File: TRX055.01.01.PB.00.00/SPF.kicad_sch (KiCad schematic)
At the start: 1 part, among them J5 SFP

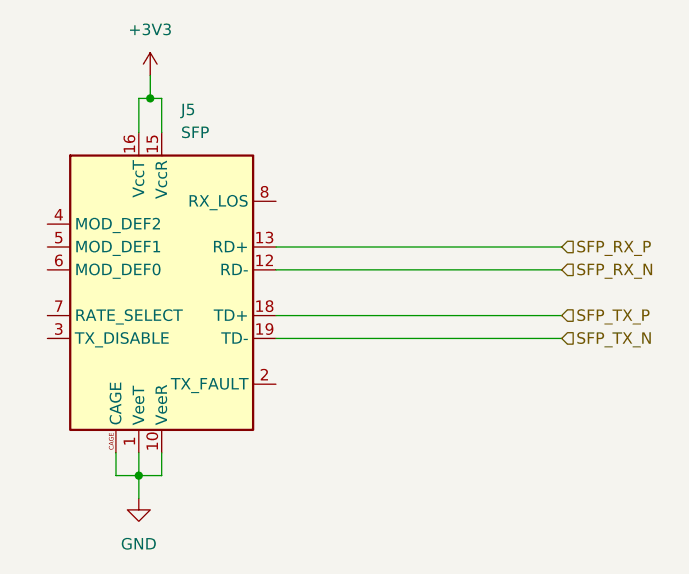
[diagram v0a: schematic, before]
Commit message: +ETH +USB +Connectors
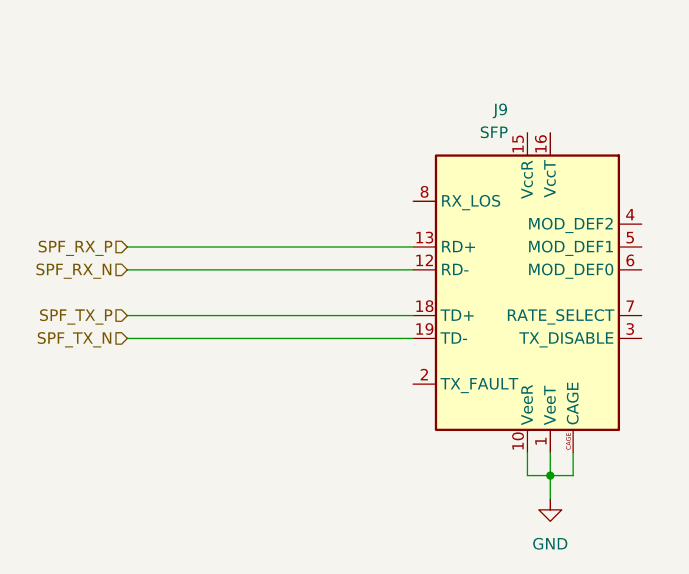
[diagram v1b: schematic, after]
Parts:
- removed J5: SFP, Connector:Connector_SFP_and_Cage, symbol Interface_Optical:SFP
- added J9: SFP, Connector:Connector_SFP_and_Cage, symbol Interface_Optical:SFP
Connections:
- net GND: now also J9.1 (VeeT), J9.10 (VeeR), J9.11 (VeeR), J9.14 (VeeR), J9.17 (VeeT), J9.20 (VeeT), J9.9 (VeeR), J9.CAGE
- new net SPF_RX_N: J9.12 (RD-)
- new net SPF_RX_P: J9.13 (RD+)
- new net SPF_TX_N: J9.19 (TD-)
- new net SPF_TX_P: J9.18 (TD+)
